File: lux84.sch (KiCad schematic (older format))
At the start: 361 parts, among them IC1 AP22802AW5-7, IC2 USBUF01W6, SW1 SW_Push, SW2 SW_Push, SW3 Rotary_Encoder_Switch, SW4 Rotary_Encoder_Switch, U1 STM32F072CBTx, U2 AP2127K-3.3, U3 IS31FL3733-TQ, U4 IS31FL3733-TQ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

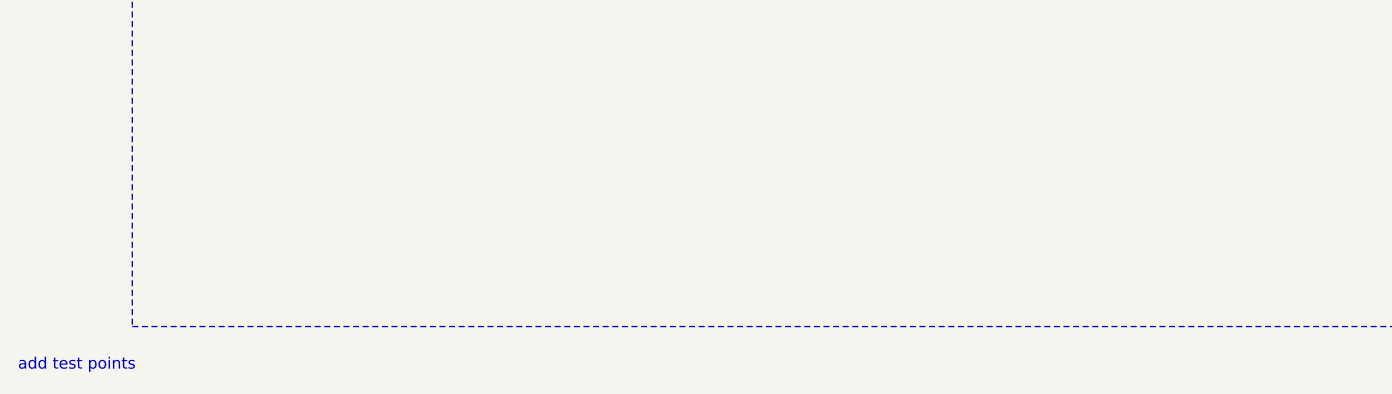
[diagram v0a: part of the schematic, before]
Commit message: Moved underglow rgb marking
Schematic is RGBA, with common anode pin 4. Part used is ABGR, with common anode pin 1.  Moved silkscreen marking to Pin 4 on PCB to denote common anode, matching the marking on the part.
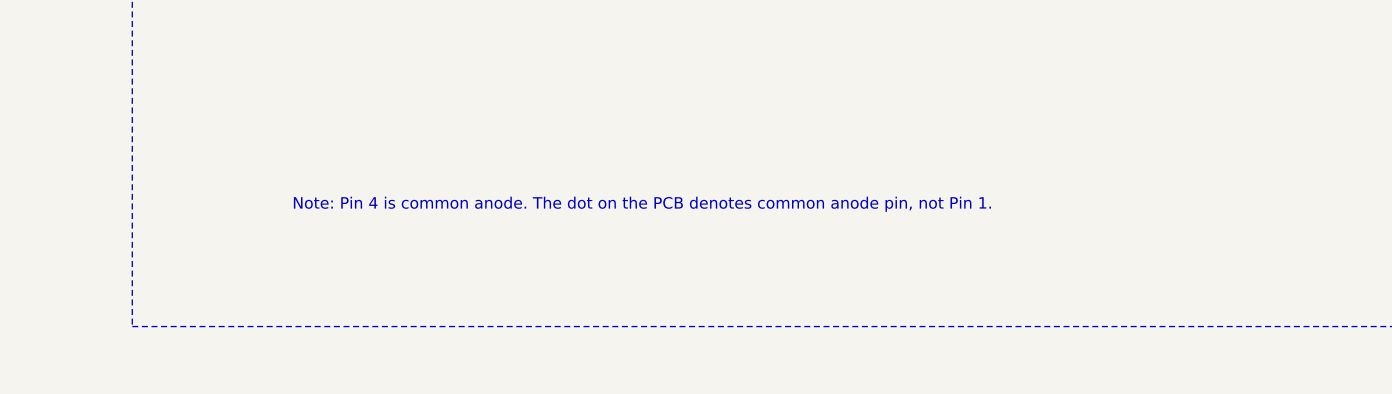
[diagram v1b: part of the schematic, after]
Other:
- note added: "Note: Pin 4 is common anode. The dot on the PCB denotes common anode pin, not Pin 1."
- note removed: "add test points"
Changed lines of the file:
@@
 EESchema Schematic File Version 4
-LIBS:Cayenne84-cache
+LIBS:lux84-cache
 EELAYER 30 0
 EELAYER END
@@
 PA1
 Connection ~ 22850 2000
-Text Notes 1100 22500 0    50   ~ 0
-add test points
 Text Label 20500 11550 2    50   ~ 0
 3.3V_LDO
@@
 	0    -1   -1   0
 $EndComp
+Text Notes 2300 21800 0    50   ~ 0
+Note: Pin 4 is common anode. The dot on the PCB denotes common anode pin, not Pin 1.
 $EndSCHEMATC
